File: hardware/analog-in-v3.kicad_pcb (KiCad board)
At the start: 2 copper layers, 30 x 35 mm, 37 parts, among them P1 CON-SENSOR2, P2 CONN_5, P3 BOOT, P4 DEBUG, U1 XMC110024, U2 TLV272IS, U3 DRILL, U4 DRILL, U5 DRILL, U6 DRILL

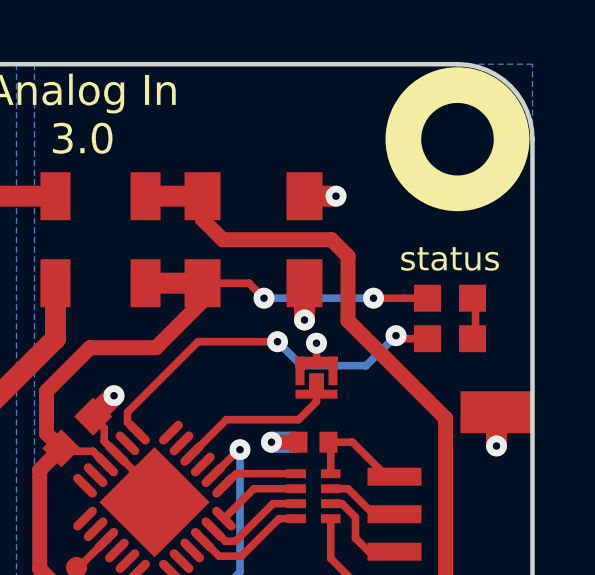
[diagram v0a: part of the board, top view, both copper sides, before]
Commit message: fix status text
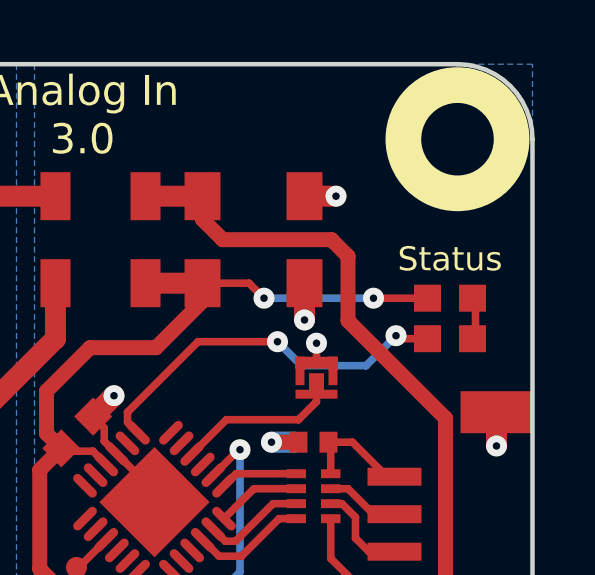
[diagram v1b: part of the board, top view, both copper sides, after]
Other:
- board text added: "Status"
- board text removed: "status"
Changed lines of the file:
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@@
     )
   )
-  (gr_text status (at 202.75 101.1) (layer F.SilkS)
+  (gr_text Status (at 202.75 101.1) (layer F.SilkS)
     (effects (font (size 0.8 0.8) (thickness 0.15)))
   )

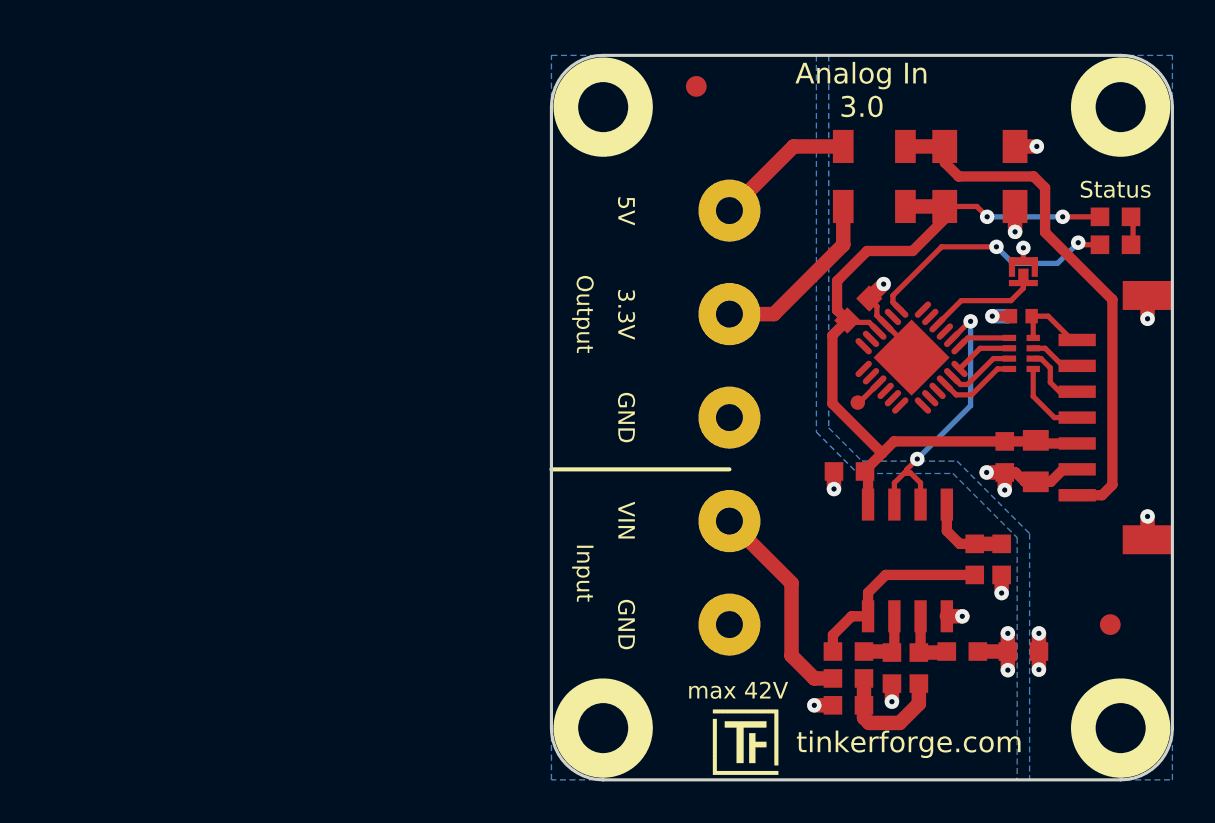
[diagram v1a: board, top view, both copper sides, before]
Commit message: New standart layout. Switched to Kicad 6
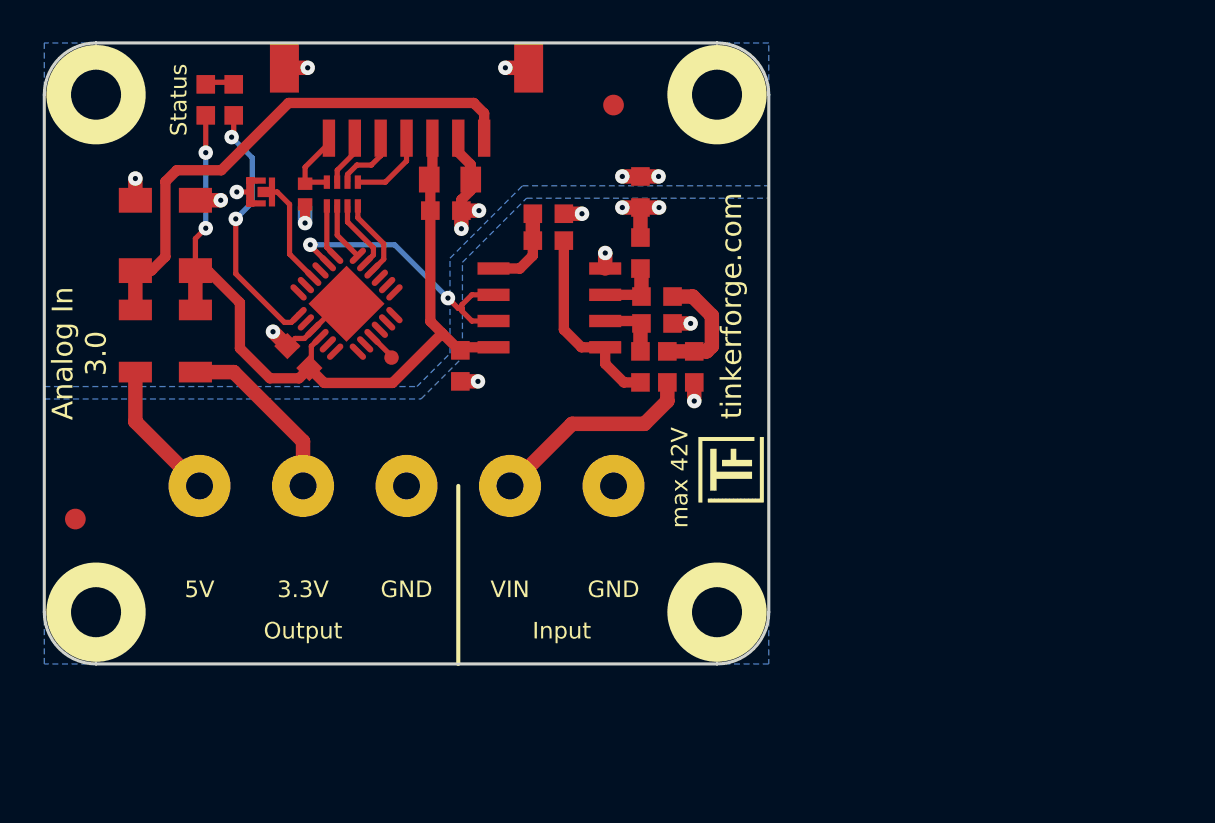
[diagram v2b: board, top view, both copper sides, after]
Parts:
- moved U6 49.5 mm to (153.5, 96.5), turned to 90 degrees
- moved D3 44.3 mm to (158.8, 96.8), turned to 90 degrees
- moved R8 43.2 mm to (160.2, 96.8), turned to 90 degrees
- moved P1 41.2 mm to (168.5, 94.0), turned to 180 degrees
- moved D2 41.0 mm to (155.4, 103.3), turned to 90 degrees
- moved D1 37.9 mm to (158.3, 103.3), turned to 90 degrees
- moved P3 37.1 mm to (161.4, 101.2), turned to 0 degrees
- moved F2 36.9 mm to (155.4, 108.4), turned to -90 degrees
- moved Fiducial_Mark 36.6 mm to (152.5, 117.0), turned to 90 degrees
- moved U5 36.3 mm to (183.5, 96.5), turned to 90 degrees
- moved C5 35.1 mm to (163.6, 101.3), turned to -90 degrees
- moved Fiducial_Mark 34.7 mm to (178.5, 97.0), turned to 90 degrees
- moved U3 34.6 mm to (153.5, 121.5), turned to 90 degrees
- moved RP1 33.7 mm to (165.4, 101.3), turned to 180 degrees
- moved F1 33.4 mm to (158.3, 108.4), turned to -90 degrees
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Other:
- board size 30 x 35 mm -> 35 x 30 mm
- net class Default removed

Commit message: Data Cleanup
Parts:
- moved C7 0.11 mm to (163.2, 109.1)
- moved C3 0.07 mm to (175.4, 102.2)
- moved R1 0.07 mm to (175.4, 103.5)
- moved R8 0.07 mm to (160.1, 96.7)
- moved P3 0.05 mm to (161.5, 101.2)
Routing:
- net GND: track 26.0 -> 25.2 mm
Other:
- rule pad_to_mask_clearance: 0.15 -> 0
- board text added: "Copyright Tinkerforge GmbH 2023. This documentation describes Open Hardware and is licensed under the CERN OHL v. 1.1. You may redistribute and modify this documentation under the terms of the CERN OHL v.1.1. (http://ohwr.org/cernohl). This documentation is distributed WITHOUT ANY EXPRESS OR IMPLIED WARRANTY, INCLUDING OF MERCHANTABILITY, SATISFACTORY QUALITY AND FITNESS FOR A PARTICULAR PURPOSE.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"
- board text removed: "Copyright Tinkerforge GmbH 2017. This documentation describes Open Hardware and is licensed under the CERN OHL v. 1.1. You may redistribute and modify this documentation under the terms of the CERN OHL v.1.1. (http://ohwr.org/cernohl). This documentation is distributed WITHOUT ANY EXPRESS OR IMPLIED WARRANTY, INCLUDING OF MERCHANTABILITY, SATISFACTORY QUALITY AND FITNESS FOR A PARTICULAR PURPOSE.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"
